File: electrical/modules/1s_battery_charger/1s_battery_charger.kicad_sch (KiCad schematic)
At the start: 26 parts, among them Q1101 CSD16570Q5B, U1101 BQ25798

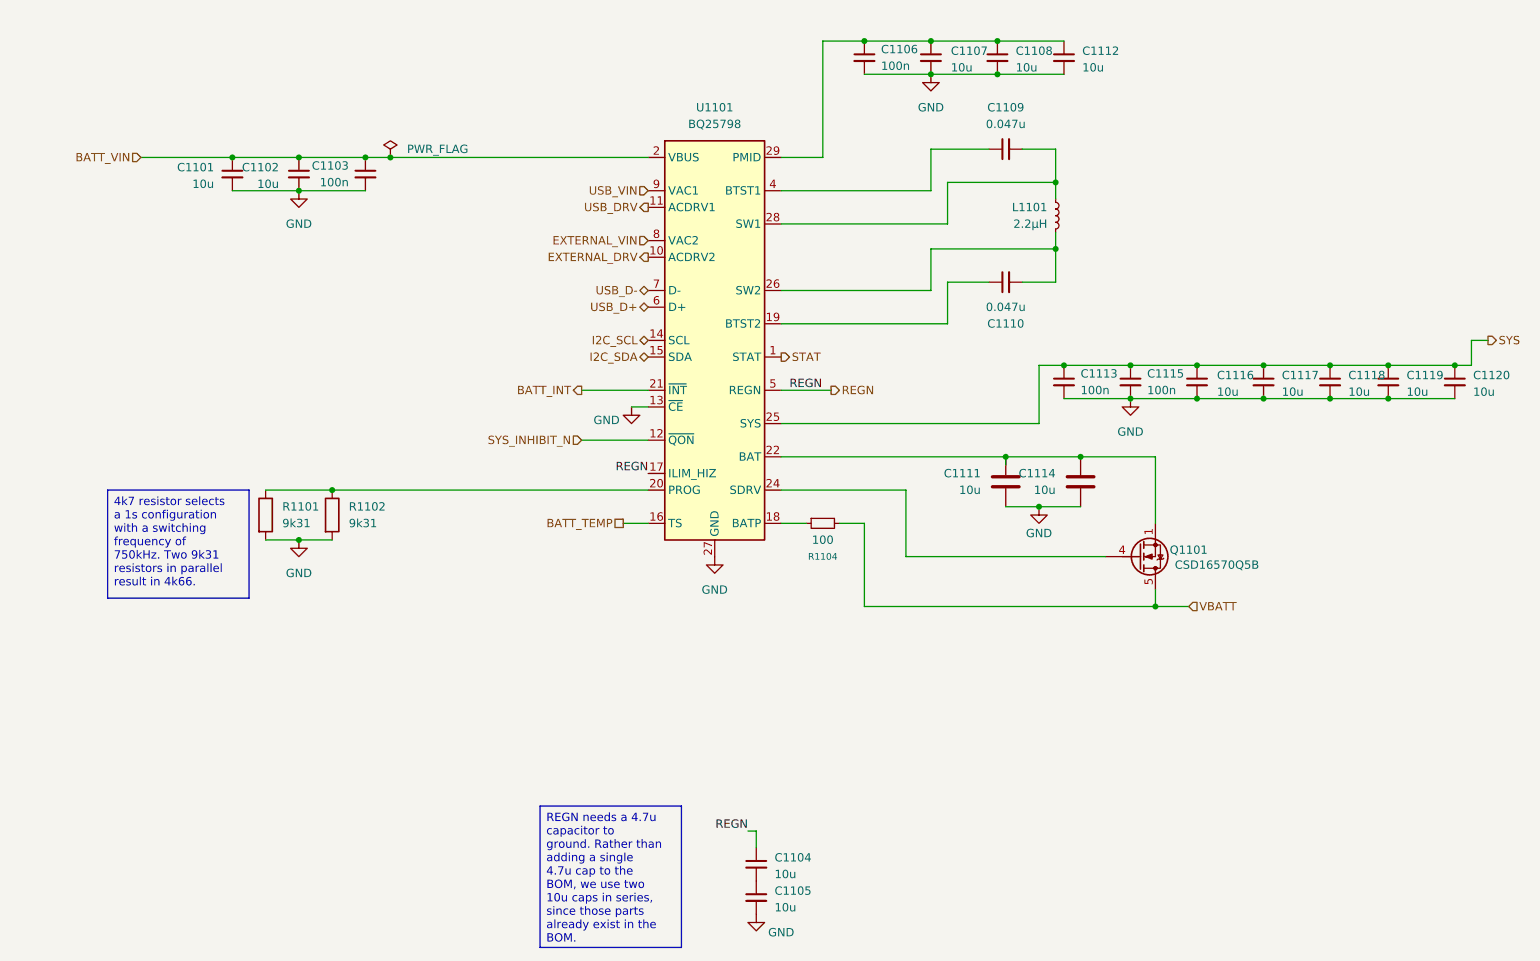
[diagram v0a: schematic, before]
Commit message: Checkpoint work on layout of 1s3p battery board. Most of the electrical connections are complete; silkscreening needs work. Also, the USB header and schematic symbol need auditing; they are not in sync and the pad numbers may not match the actual header.
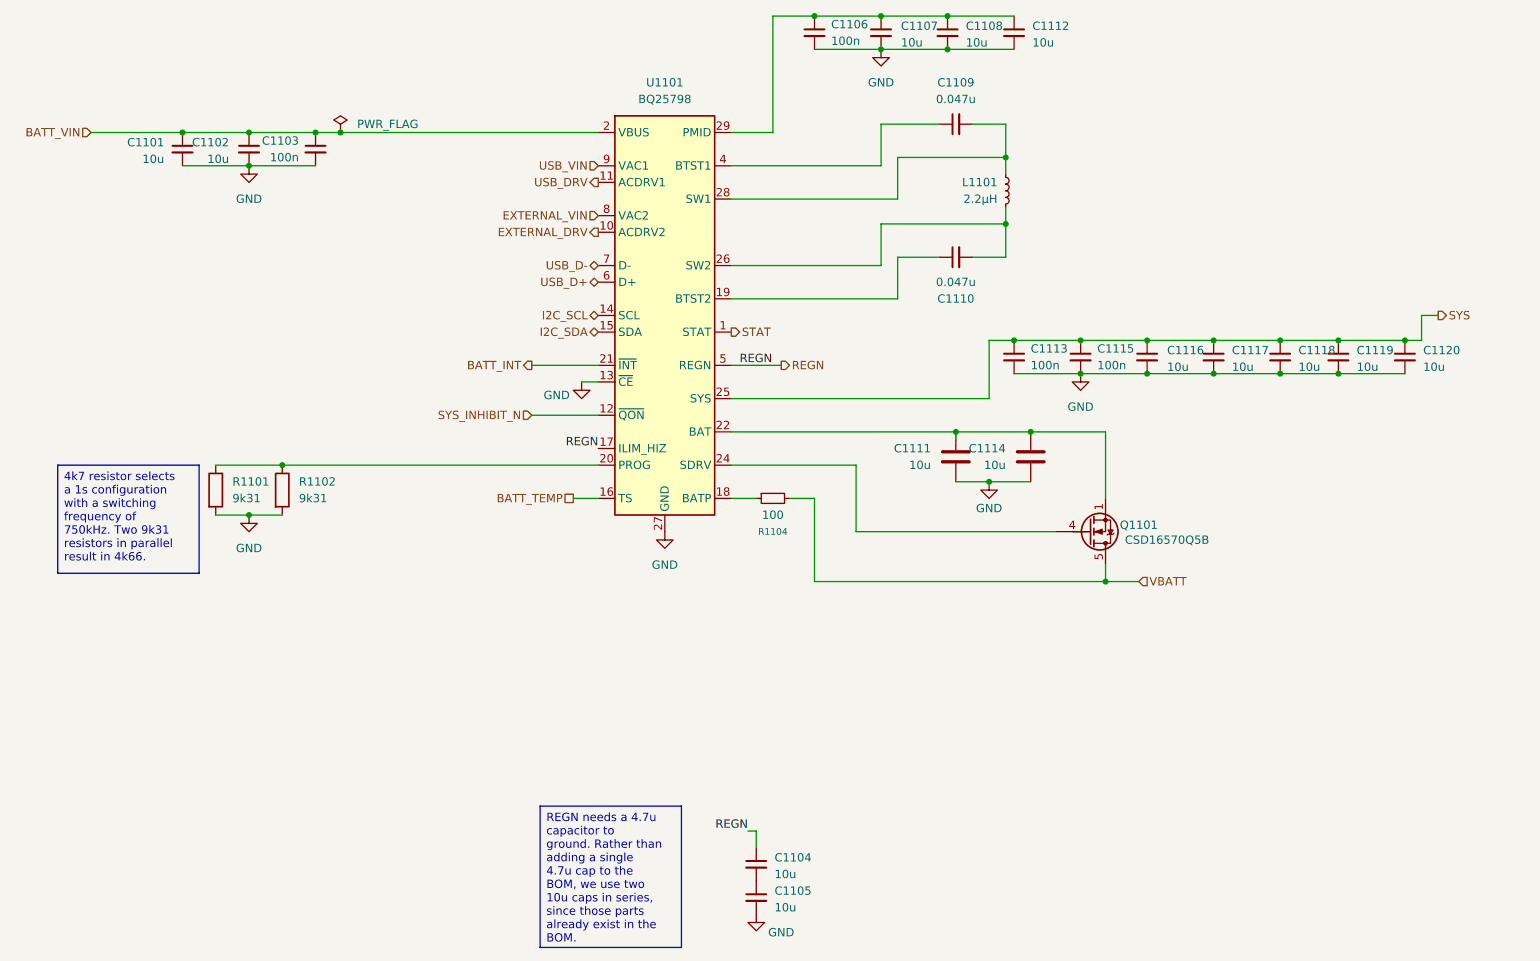
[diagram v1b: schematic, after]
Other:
- moved on the sheet: C1101, C1102, C1103, C1106, C1107, C1108, C1109, C1110, C1111, C1112, C1113, C1114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
